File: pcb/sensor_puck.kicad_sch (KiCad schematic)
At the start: 71 parts, among them J1 DISP LEFT, J2 DISP RIGHT, J3 USB_C_Receptacle_USB2.0_16P, J5 Generic, Q1 2N7002, SW1 RST, SW2 BOOT, U1 ESP32-S3-MINI-1U, U2 ST25DV16K-IER8C3, U3 LSM6DSOXTR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

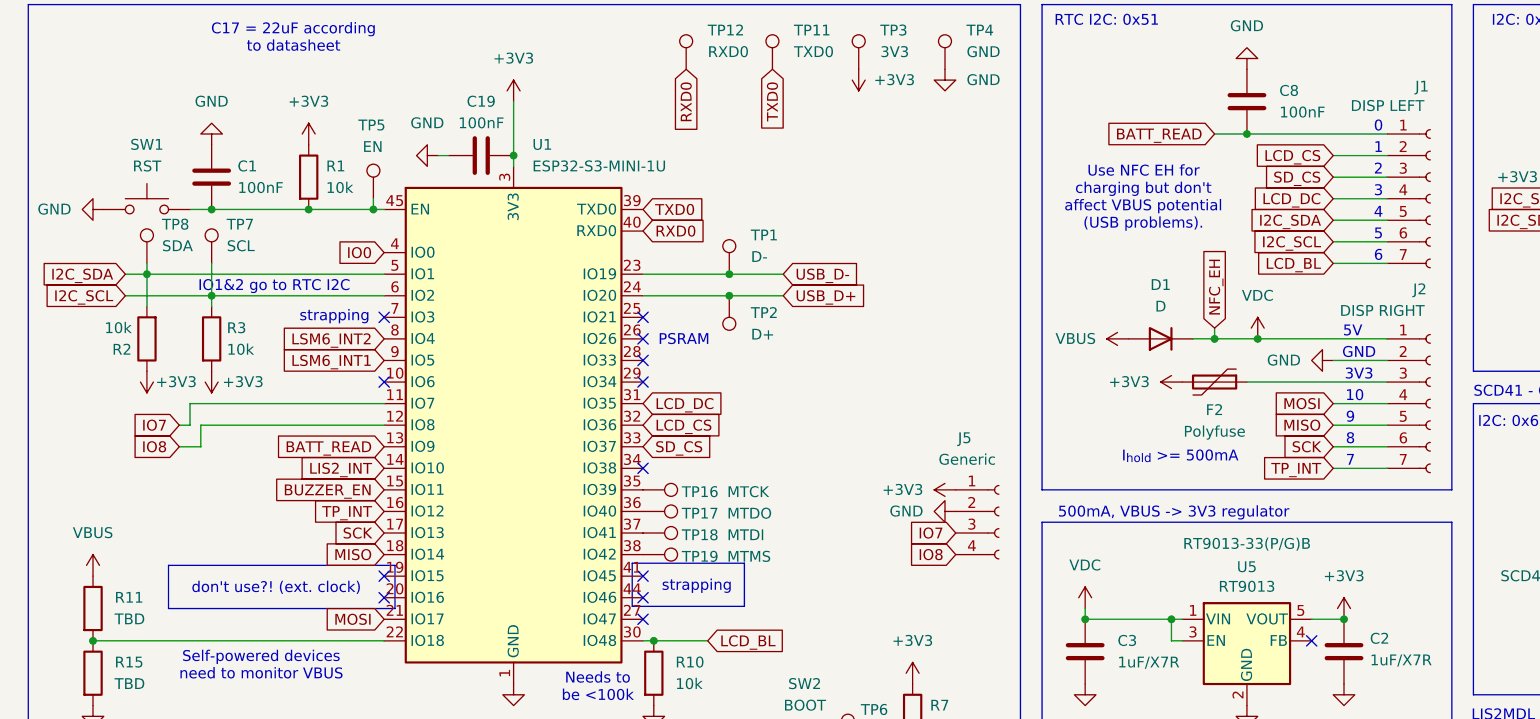
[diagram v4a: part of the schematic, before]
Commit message: feat(schematic): connect display using separate I2C bus
Since we're polling at least the LSM very fast, the constantly busy bus
might cause us to detect touch slower, thereby making the user
experience with the display worse. By putting the touch screen sensor
onto its own I2C bus, we might be able to avoid this. Note that this
works, since the ESP has two I2C controllers, that can be routed to any
pin (as far as I understand).
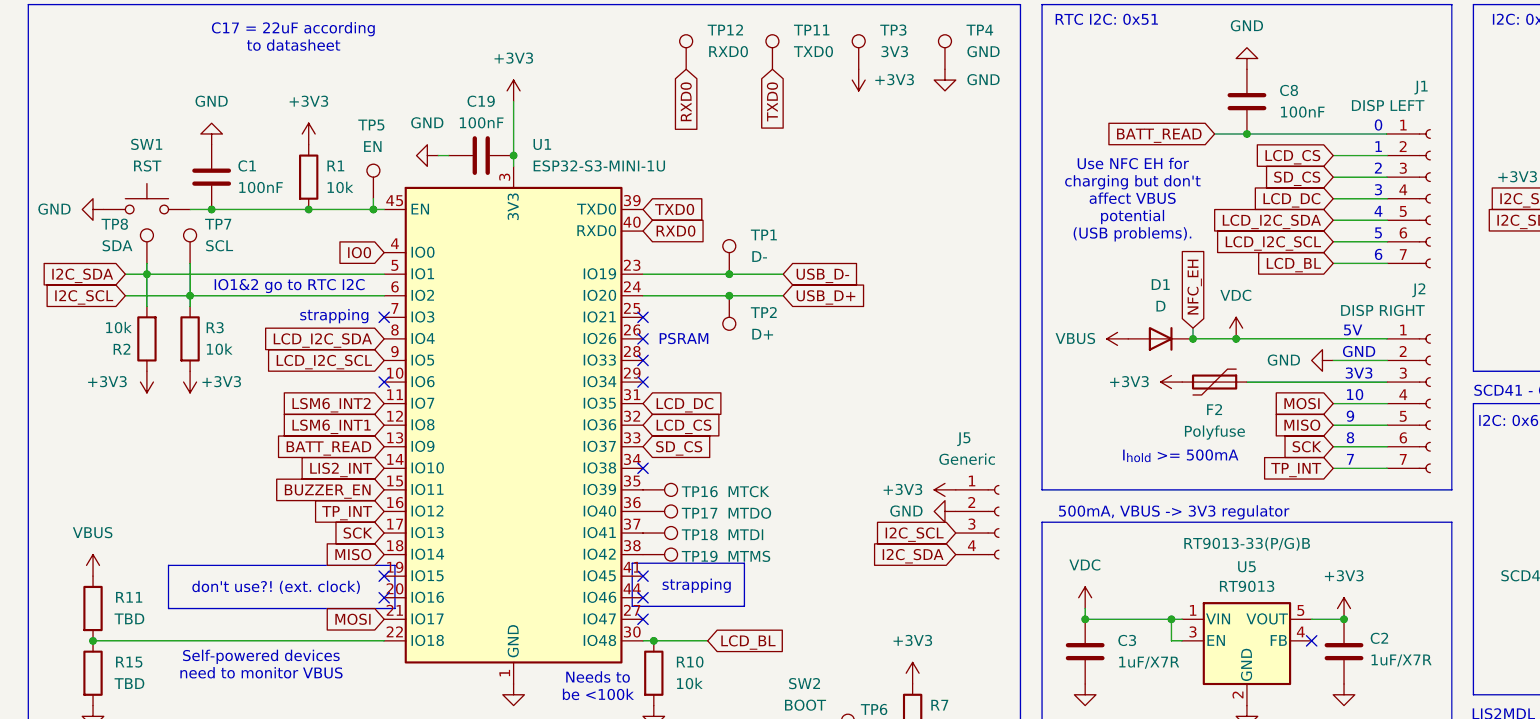
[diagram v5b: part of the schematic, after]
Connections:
- net I2C_SCL: now also J5.3 (Pin_3); no longer J1.6 (Pin_6)
- net I2C_SDA: now also J5.4 (Pin_4); no longer J1.5 (Pin_5)
- net LSM6_INT1: now also U1.12 (IO8); no longer U1.9 (IO5)
- net LSM6_INT2: now also U1.11 (IO7); no longer U1.8 (IO4)
- removed net IO7: J5.3 (Pin_3), U1.11 (IO7)
- removed net IO8: J5.4 (Pin_4), U1.12 (IO8)
- new net LCD_I2C_SCL: J1.6 (Pin_6), U1.9 (IO5)
- new net LCD_I2C_SDA: J1.5 (Pin_5), U1.8 (IO4)
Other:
- moved on the sheet: R3, TP7

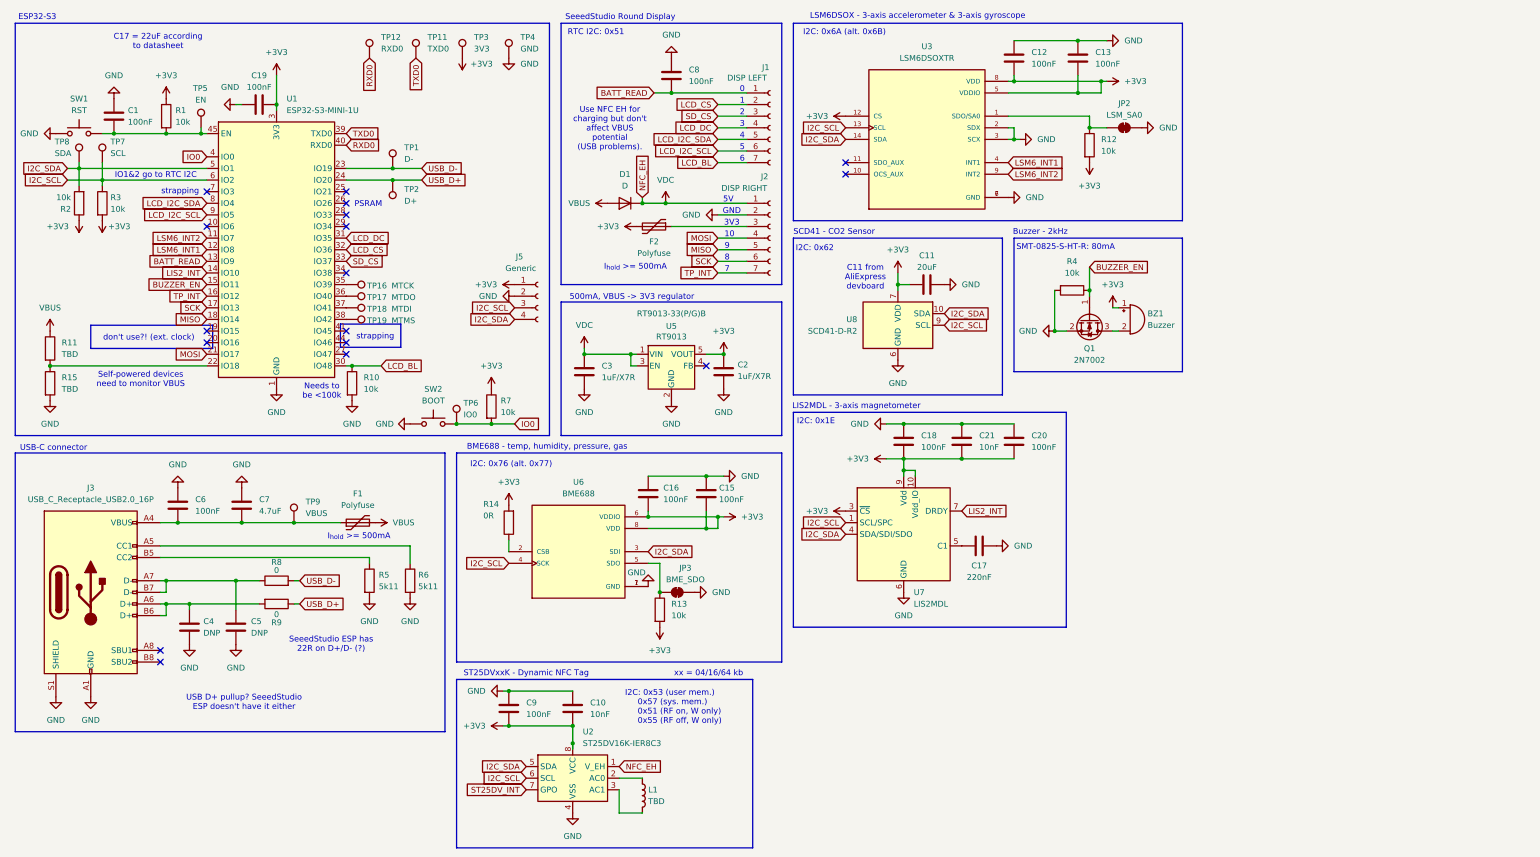
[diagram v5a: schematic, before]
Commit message: fix(schematic): add pullups to LCD I2C lines
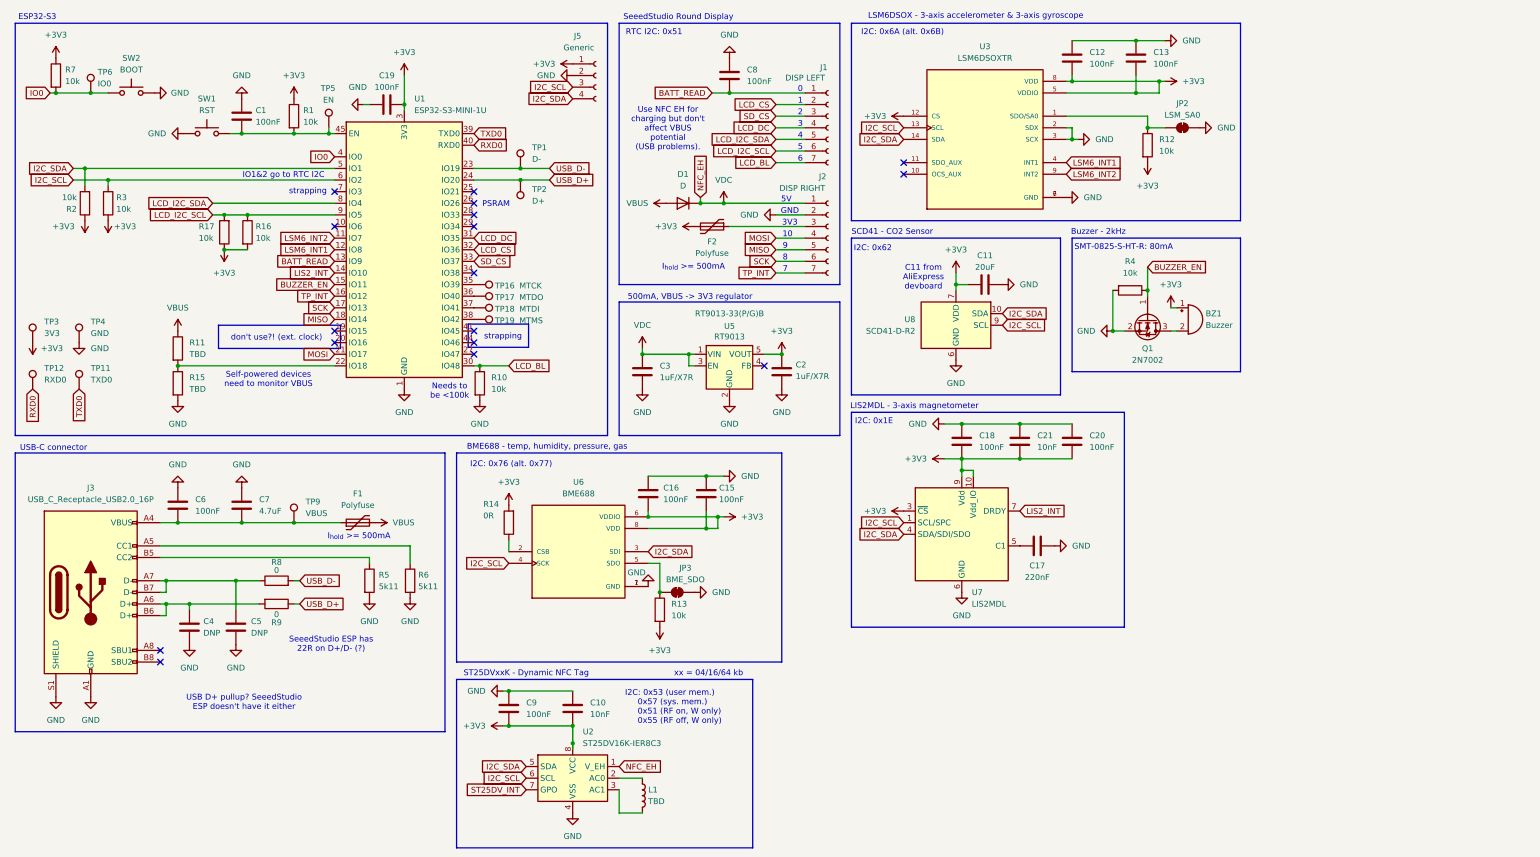
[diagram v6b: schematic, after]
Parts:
- removed TP7: SCL, TestPoint:TestPoint_Pad_D1.0mm, symbol Connector:TestPoint
- removed TP8: SDA, TestPoint:TestPoint_Pad_D1.0mm, symbol Connector:TestPoint
- added R16, R17: 10k, symbol Device:R
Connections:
- net +3V3: now also R16.2, R17.1
- net GND: now also SW2.2; no longer SW2.1
- net IO0: now also SW2.1; no longer SW2.2
- net LCD_I2C_SCL: now also R16.1, R17.2
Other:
- note removed: "C17 = 22uF according to datasheet"
- moved on the sheet: BZ1, C1, C11, C12, C13, C17, C18, C19, C2, C20, C21, C3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

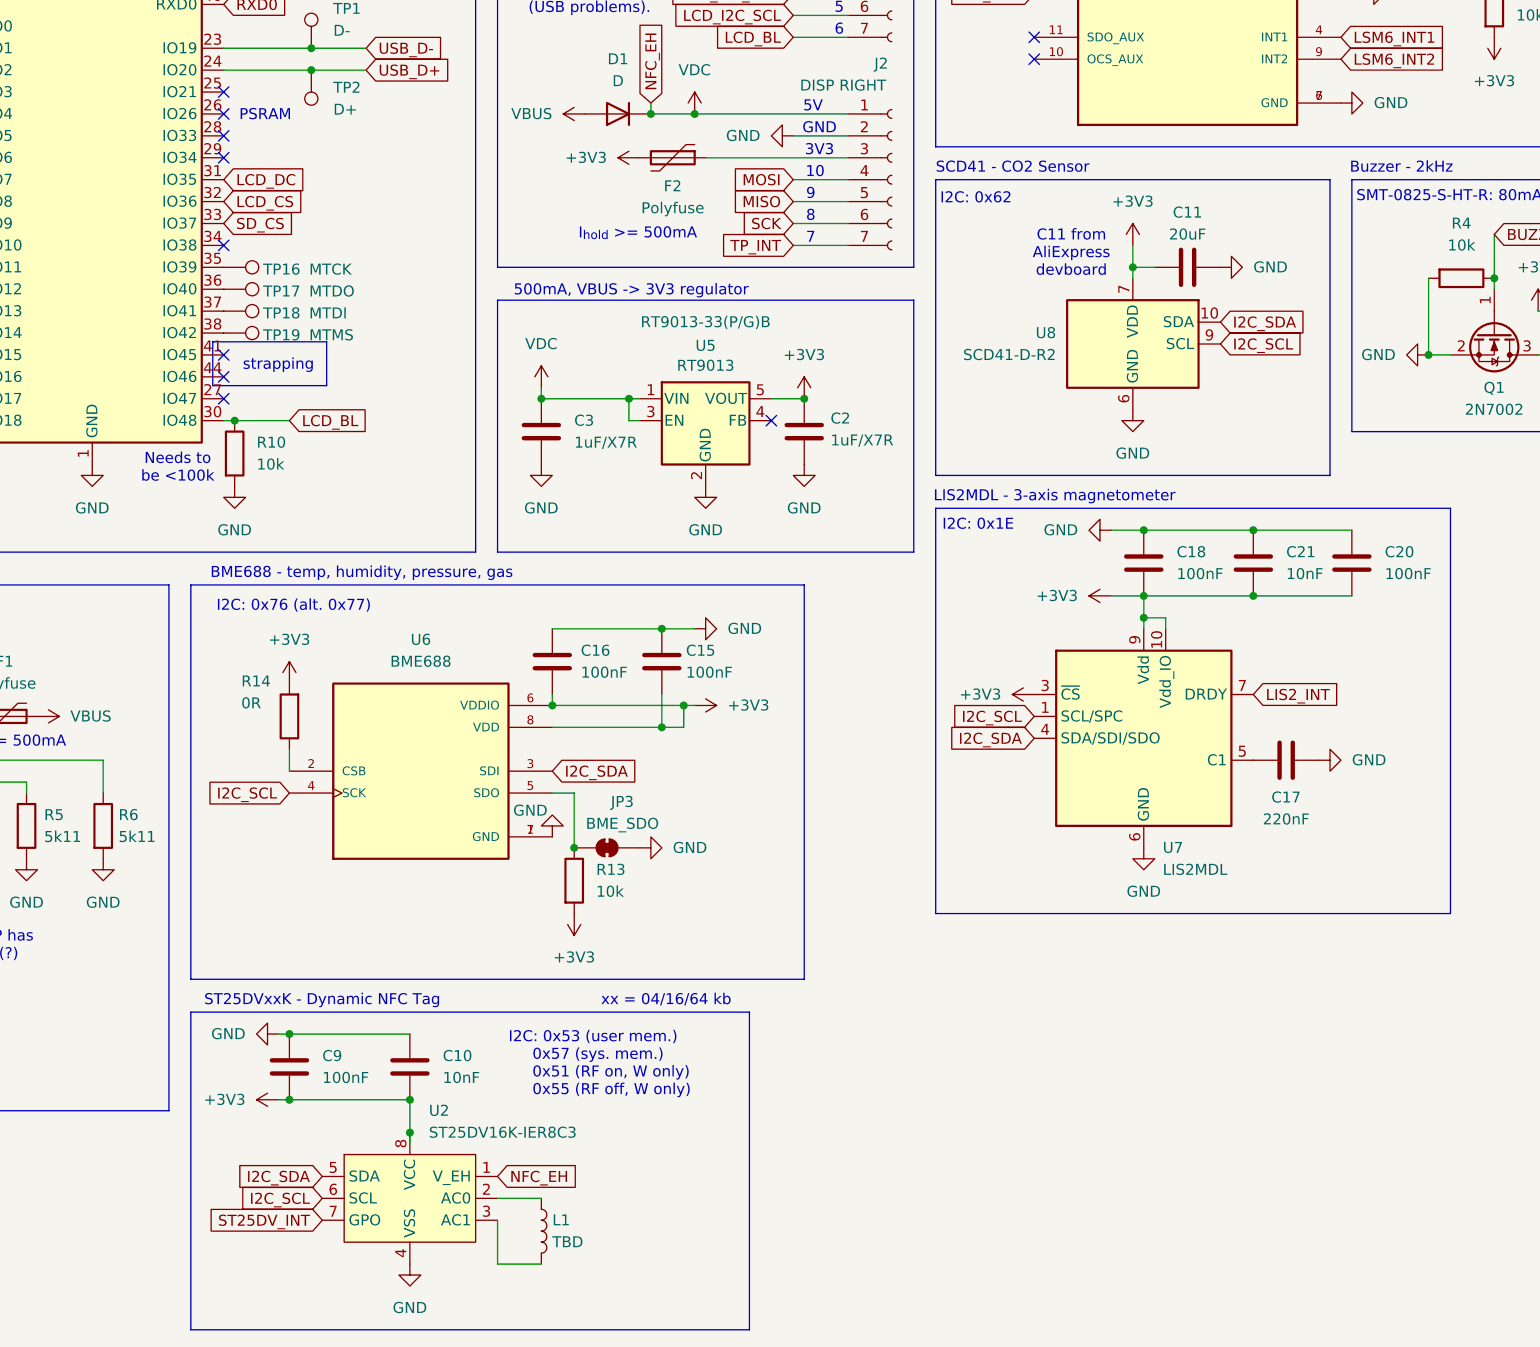
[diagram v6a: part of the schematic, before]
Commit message: feat(schematic): remove unnecessary BME688
The BME688 we previously had on the PCB has gotten kind of useless,
since the SCD41 already has a temperature and humidity sensor on board.
This means the BME could only give us pressure (which, as the user, you
can't really do much with in my opinion), or VOC gas measurements,
which, to really do anything with, we'd need to use that BSEC library,
which feels kind of sketchy with the way its licensed.
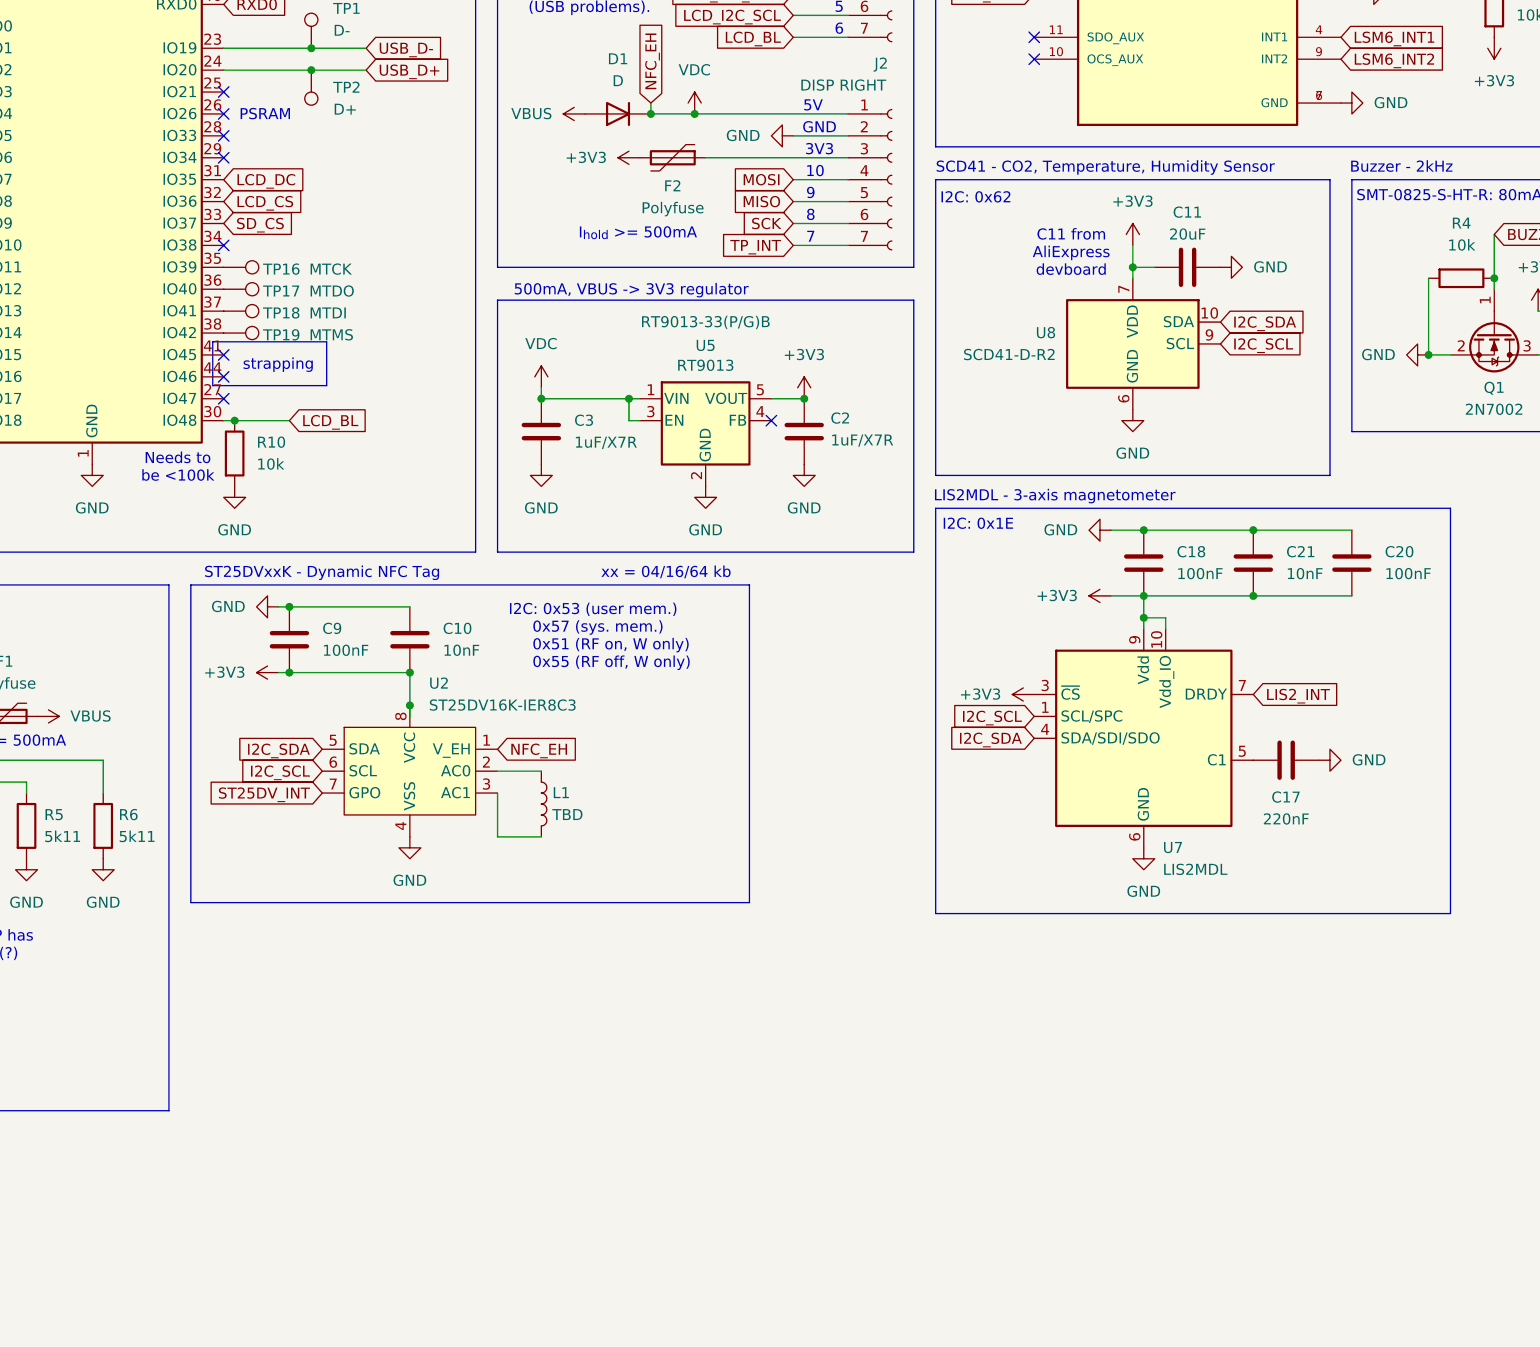
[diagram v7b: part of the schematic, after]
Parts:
- removed C15, C16: 100nF, Capacitor_SMD:C_0805_2012Metric, symbol Device:C
- removed JP3: BME_SDO, Jumper:SolderJumper-2_P1.3mm_Bridged_RoundedPad1.0x1.5mm, symbol Jumper:SolderJumper_2_Bridged
- removed R13: 10k, Resistor_SMD:R_0805_2012Metric, symbol Device:R
- removed R14: 0R, Resistor_SMD:R_0805_2012Metric, symbol Device:R
- removed U6: BME688, BME688:IC_BME688, symbol BME688:BME688
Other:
- note added: "SCD41 - CO2, Temperature, Humidity Sensor"
- note removed: "BME688 - temp, humidity, pressure, gas"
- note removed: "I2C: 0x76 (alt. 0x77)"
- note removed: "SCD41 - CO2 Sensor"
- moved on the sheet: C10, C9, L1, U2

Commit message: chore: remove unused code and clean up
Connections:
- net VDC: no longer U2.1 (V_EH)
- no-connect marks 17 -> 18
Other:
- note removed: "Use NFC EH for charging but don't affect VBUS potential (USB problems)."
